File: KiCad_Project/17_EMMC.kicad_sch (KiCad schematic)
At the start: 15 parts, among them U6 SDINBDG4-8G

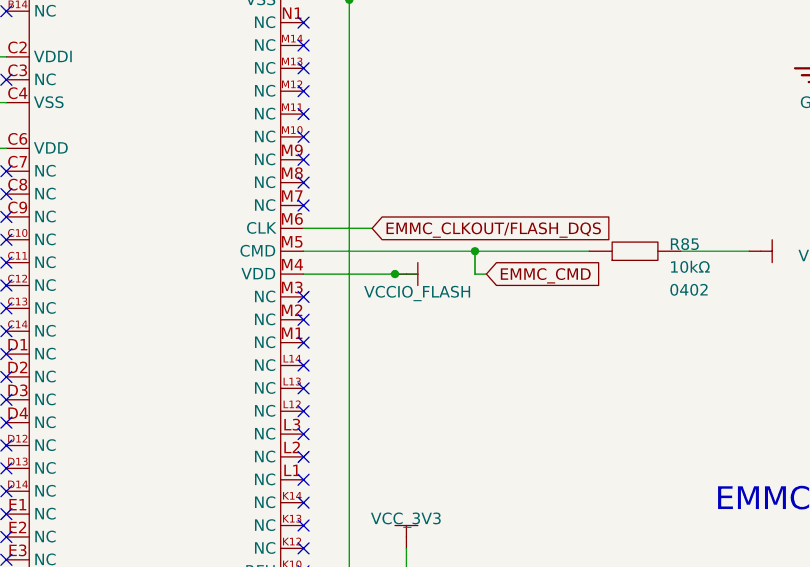
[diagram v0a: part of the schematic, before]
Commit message: Update additional PCBs
Add WIFI PCB to get best antenna
Add Display Debbugger to get interface pinout
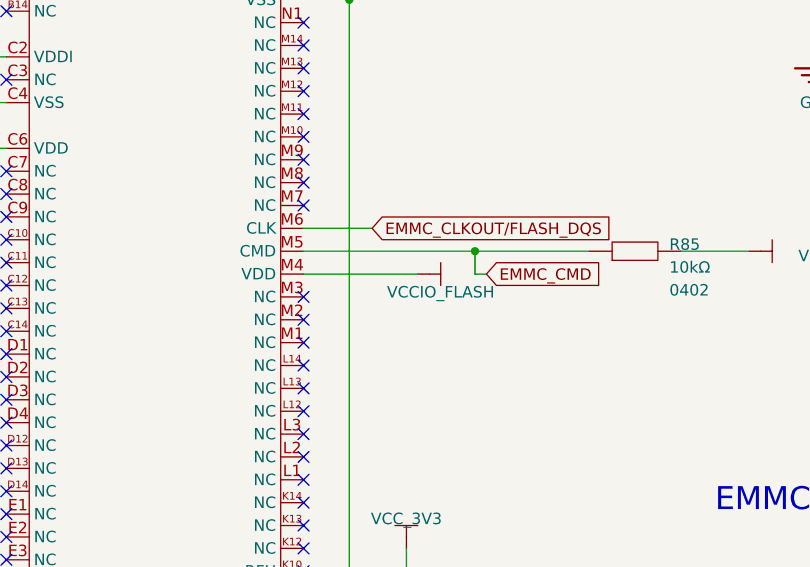
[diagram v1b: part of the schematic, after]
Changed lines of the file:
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@@
 	)
 	(junction
-		(at 226.06 134.62)
-		(diameter 0)
-		(color 0 0 0 0)
-	)
-	(junction
 		(at 298.45 68.58)
 		(diameter 0)
@@
 	(wire
 		(pts
-			(xy 226.06 134.62) (xy 215.9 134.62)
+			(xy 215.9 134.62) (xy 228.6 134.62)
 		)
 		(stroke
@@
 	(wire
 		(pts
-			(xy 228.6 134.62) (xy 226.06 134.62)
-		)
-		(stroke
-			(width 0)
-			(type default)
-		)
-	)
-	(wire
-		(pts
 			(xy 215.9 132.08) (xy 234.95 132.08)
 		)
@@
 	(symbol
 		(lib_id "LCSC Taish-easyedapro:Power-VCC")
-		(at 226.06 134.62 270)
+		(at 228.6 134.62 270)
 		(unit 1)
 		(exclude_from_sim no)
@@
 		(dnp no)
 		(property "Reference" "#PWR0268"
-			(at 226.06 134.62 0)
+			(at 228.6 134.62 0)
 			(effects
 				(font
@@
 		)
 		(property "Value" "VCCIO_FLASH"
-			(at 228.6 135.89 90)
+			(at 231.14 135.89 90)
 			(effects
 				(font
@@
 		)
 		(property "Footprint" "LCSC Taish-easyedapro:"
-			(at 226.06 134.62 0)
+			(at 228.6 134.62 0)
 			(effects
 				(font
@@
 		)
 		(property "Datasheet" ""
-			(at 226.06 134.62 0)
+			(at 228.6 134.62 0)
 			(effects
 				(font
@@
 		)
 		(property "Description" ""
-			(at 226.06 134.62 0)
+			(at 228.6 134.62 0)
 			(effects
 				(font
